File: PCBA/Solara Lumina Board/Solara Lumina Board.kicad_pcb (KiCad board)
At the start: 2 copper layers, 72.5 x 54 mm, 0 parts

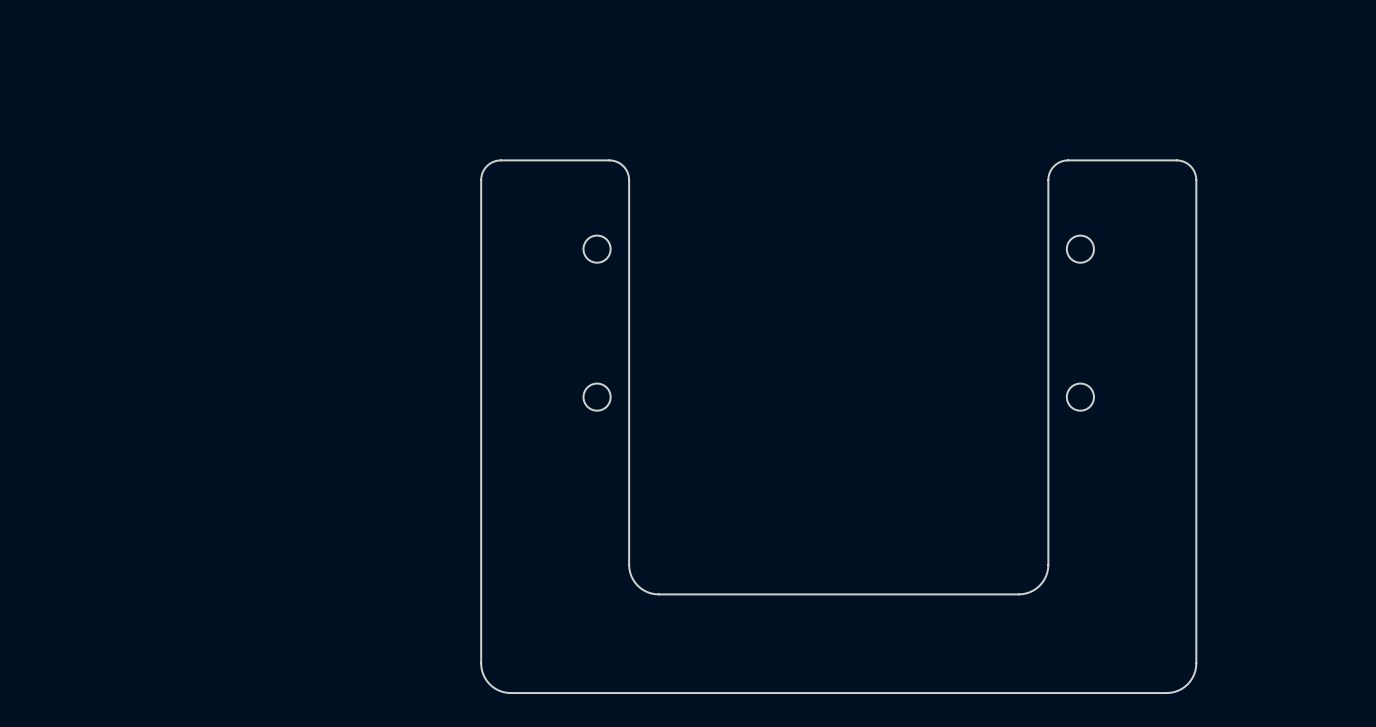
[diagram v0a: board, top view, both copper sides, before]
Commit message: Updated outline
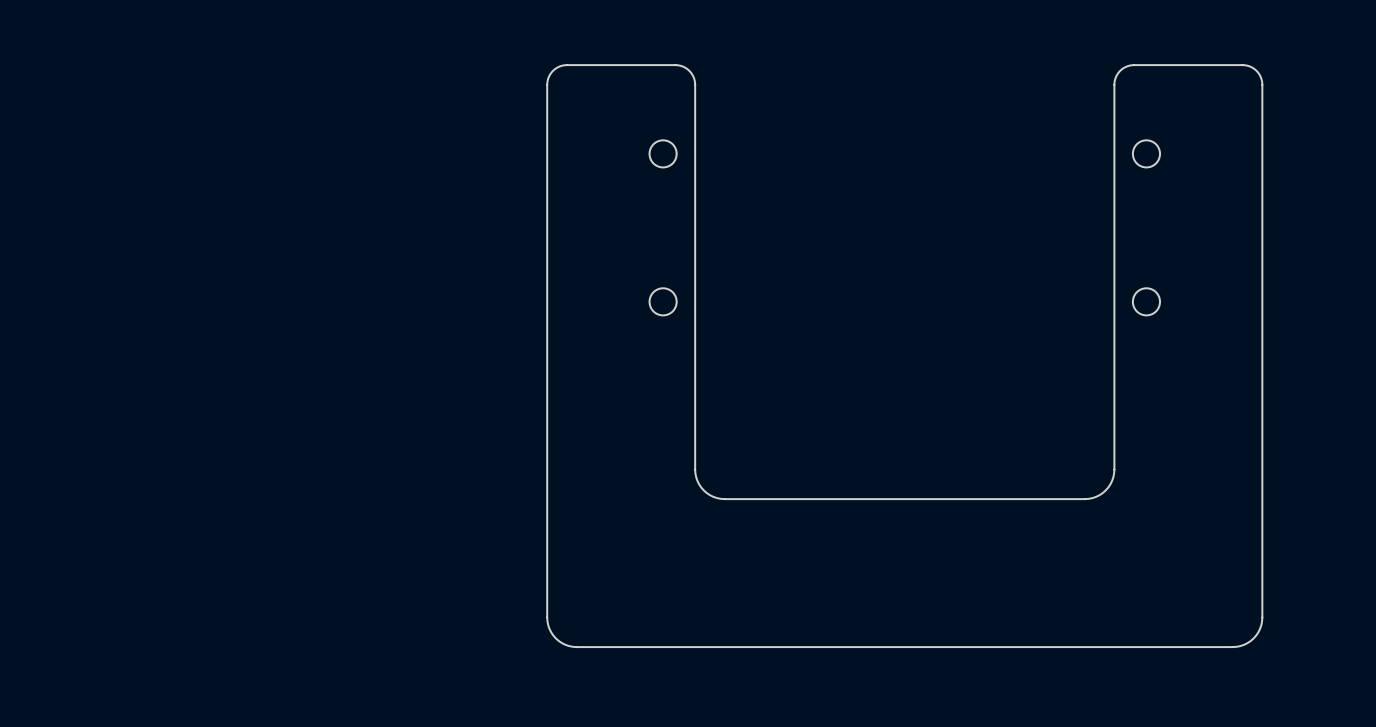
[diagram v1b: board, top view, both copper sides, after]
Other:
- board size 72.5 x 54 mm -> 72.5 x 59 mm
- copper layers 2 -> 6
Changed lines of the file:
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@@
 	(layers
 		(0 "F.Cu" signal)
+		(1 "In1.Cu" signal)
+		(2 "In2.Cu" signal)
+		(3 "In3.Cu" signal)
+		(4 "In4.Cu" signal)
 		(31 "B.Cu" signal)
 		(32 "B.Adhes" user "B.Adhesive")
@@
 	)
 	(setup
+		(stackup
+			(layer "F.SilkS"
+				(type "Top Silk Screen")
+			)
+			(layer "F.Paste"
+				(type "Top Solder Paste")
+			)
+			(layer "F.Mask"
+				(type "Top Solder Mask")
+				(color "White")
+				(thickness 0.01)
+			)
+			(layer "F.Cu"
+				(type "copper")
+				(thickness 0.035)
+			)
+			(layer "dielectric 1"
+				(type "prepreg")
+				(thickness 0.1)
+				(material "FR4")
+				(epsilon_r 4.5)
+				(loss_tangent 0.02)
+			)
+			(layer "In1.Cu"
+				(type "copper")
+				(thickness 0.035)
+			)
+			(layer "dielectric 2"
+				(type "core")
+				(thickness 0.535)
+				(material "FR4")
+				(epsilon_r 4.5)
+				(loss_tangent 0.02)
+			)
+			(layer "In2.Cu"
+				(type "copper")
+				(thickness 0.035)
+			)
+			(layer "dielectric 3"
+				(type "prepreg")
+				(thickness 0.1)
+				(material "FR4")
+				(epsilon_r 4.5)
+				(loss_tangent 0.02)
+			)
+			(layer "In3.Cu"
+				(type "copper")
+				(thickness 0.035)
+			)
+			(layer "dielectric 4"
+				(type "core")
+				(thickness 0.535)
+				(material "FR4")
+				(epsilon_r 4.5)
+				(loss_tangent 0.02)
+			)
+			(layer "In4.Cu"
+				(type "copper")
+				(thickness 0.035)
+			)
+			(layer "dielectric 5"
+				(type "prepreg")
+				(thickness 0.1)
+				(material "FR4")
+				(epsilon_r 4.5)
+				(loss_tangent 0.02)
+			)
+			(layer "B.Cu"
+				(type "copper")
+				(thickness 0.035)
+			)
+			(layer "B.Mask"
+				(type "Bottom Solder Mask")
+				(color "White")
+				(thickness 0.01)
+			)
+			(layer "B.Paste"
+				(type "Bottom Solder Paste")
+			)
+			(layer "B.SilkS"
+				(type "Bottom Silk Screen")
+			)
+			(copper_finish "None")
+			(dielectric_constraints no)
+		)
 		(pad_to_mask_clearance 0)
 		(allow_soldermask_bridges_in_footprints no)
@@
 	(net 0 "")
 	(gr_line
-		(start 177.18 71.660002)
-		(end 166.18 71.660002)
-		(stroke
-			(width 0.2)
-			(type default)
-		)
-		(layer "Edge.Cuts")
-	)
-	(gr_line
-		(start 164.18 73.660002)
-		(end 164.18 112.660002)
+		(start 167.875 106)
+		(end 131.375001 106)
+		(stroke
+			(width 0.2)
+			(type default)
+		)
+		(layer "Edge.Cuts")
+	)
+	(gr_arc
+		(start 116.375001 121)
+		(mid 114.25368 120.12132)
+		(end 113.375 117.999999)
+		(stroke
+			(width 0.2)
+			(type default)
+		)
+		(layer "Edge.Cuts")
+	)
+	(gr_arc
+		(start 126.375001 62)
+		(mid 127.789214 62.585786)
+		(end 128.375 63.999999)
+		(stroke
+			(width 0.2)
+			(type default)
+		)
+		(layer "Edge.Cuts")
+	)
+	(gr_arc
+		(start 131.375001 106)
+		(mid 129.25368 105.12132)
+		(end 128.375 102.999999)
+		(stroke
+			(width 0.2)
+			(type default)
+		)
+		(layer "Edge.Cuts")
+	)
+	(gr_arc
+		(start 183.875 62)
+		(mid 185.289214 62.585786)
+		(end 185.875 64)
+		(stroke
+			(width 0.2)
+			(type default)
+		)
+		(layer "Edge.Cuts")
+	)
+	(gr_line
+		(start 183.875 62)
+		(end 172.875 62)
+		(stroke
+			(width 0.2)
+			(type default)
+		)
+		(layer "Edge.Cuts")
+	)
+	(gr_line
+		(start 170.875 64)
+		(end 170.875 103)
+		(stroke
+			(width 0.2)
+			(type default)
+		)
+		(layer "Edge.Cuts")
+	)
+	(gr_arc
+		(start 170.875 103)
+		(mid 169.99632 105.12132)
+		(end 167.875 106)
 		(stroke
 			(width 0.2)
@@
 	)
 	(gr_circle
-		(center 118.43 80.660002)
-		(end 119.805 80.660002)
+		(center 174.125 71)
+		(end 175.5 71)
 		(stroke
 			(width 0.2)
@@
 		(layer "Edge.Cuts")
 	)
-	(gr_arc
-		(start 119.680001 71.660002)
-		(mid 121.094214 72.245788)
-		(end 121.68 73.660001)
-		(stroke
-			(width 0.2)
-			(type default)
-		)
-		(layer "Edge.Cuts")
-	)
-	(gr_arc
-		(start 106.68 73.66)
-		(mid 107.265786 72.245788)
-		(end 108.679998 71.660002)
-		(stroke
-			(width 0.2)
-			(type default)
-		)
-		(layer "Edge.Cuts")
-	)
-	(gr_line
-		(start 179.18 122.660002)
-		(end 179.18 73.660002)
-		(stroke
-			(width 0.2)
-			(type default)
-		)
-		(layer "Edge.Cuts")
-	)
-	(gr_line
-		(start 109.680001 125.660002)
-		(end 176.18 125.660002)
+	(gr_line
+		(start 185.875 118)
+		(end 185.875 64)
+		(stroke
+			(width 0.2)
+			(type default)
+		)
+		(layer "Edge.Cuts")
+	)
+	(gr_arc
+		(start 185.875 118)
+		(mid 184.99632 120.12132)
+		(end 182.875 121)
+		(stroke
+			(width 0.2)
+			(type default)
+		)
+		(layer "Edge.Cuts")
+	)
+	(gr_line
+		(start 113.375 63.999999)
+		(end 113.375 117.999999)
+		(stroke
+			(width 0.2)
+			(type default)
+		)
+		(layer "Edge.Cuts")
+	)
+	(gr_arc
+		(start 170.875 64)
+		(mid 171.460786 62.585786)
+		(end 172.875 62)
+		(stroke
+			(width 0.2)
+			(type default)
+		)
+		(layer "Edge.Cuts")
+	)
+	(gr_line
+		(start 116.375001 121)
+		(end 182.875 121)
+		(stroke
+			(width 0.2)
+			(type default)
+		)
+		(layer "Edge.Cuts")
+	)
+	(gr_line
+		(start 128.375 102.999999)
+		(end 128.375 63.999999)
+		(stroke
+			(width 0.2)
+			(type default)
+		)
+		(layer "Edge.Cuts")
+	)
+	(gr_arc
+		(start 113.375 63.999999)
+		(mid 113.960786 62.585786)
+		(end 115.374998 62)
 		(stroke
 			(width 0.2)
@@
 	)
 	(gr_circle
-		(center 167.43 95.660002)
-		(end 168.805 95.660002)
+		(center 125.125 86)
+		(end 126.5 86)
 		(stroke
 			(width 0.2)
@@
 		(layer "Edge.Cuts")
 	)
-	(gr_line
-		(start 121.68 112.660001)
-		(end 121.68 73.660001)
-		(stroke
-			(width 0.2)
-			(type default)
-		)
-		(layer "Edge.Cuts")
-	)
-	(gr_arc
-		(start 179.18 122.660002)
-		(mid 178.30132 124.781322)
-		(end 176.18 125.660002)
-		(stroke
-			(width 0.2)
-			(type default)
-		)
-		(layer "Edge.Cuts")
-	)
-	(gr_line
-		(start 161.18 115.660002)
-		(end 124.680001 115.660002)
-		(stroke
-			(width 0.2)
-			(type default)
-		)
-		(layer "Edge.Cuts")
-	)
-	(gr_arc
-		(start 164.18 73.660002)
-		(mid 164.765786 72.245788)
-		(end 166.18 71.660002)
-		(stroke
-			(width 0.2)
-			(type default)
-		)
-		(layer "Edge.Cuts")
-	)
-	(gr_arc
-		(start 124.680001 115.660002)
-		(mid 122.55868 114.781322)
-		(end 121.68 112.660001)
-		(stroke
-			(width 0.2)
-			(type default)
-		)
-		(layer "Edge.Cuts")
-	)
-	(gr_line
-		(start 119.680001 71.660002)
-		(end 108.679998 71.660002)
-		(stroke
-			(width 0.2)
-			(type default)
-		)
-		(layer "Edge.Cuts")
-	)
-	(gr_arc
-		(start 164.18 112.660002)
-		(mid 163.30132 114.781322)
-		(end 161.18 115.660002)
-		(stroke
-			(width 0.2)
-			(type default)
-		)
-		(layer "Edge.Cuts")
-	)
-	(gr_line
-		(start 106.68 73.66)
-		(end 106.68 122.660001)
-		(stroke
-			(width 0.2)
-			(type default)
-		)
-		(layer "Edge.Cuts")
-	)
-	(gr_arc
-		(start 177.18 71.660002)
-		(mid 178.594214 72.245788)
-		(end 179.18 73.660002)
-		(stroke
-			(width 0.2)
-			(type default)
-		)
-		(layer "Edge.Cuts")
-	)
 	(gr_circle
-		(center 167.43 80.660002)
-		(end 168.805 80.660002)
+		(center 125.125 71)
+		(end 126.5 71)
 		(stroke
 			(width 0.2)
@@
 		(layer "Edge.Cuts")
 	)
+	(gr_line
+		(start 126.375001 62)
+		(end 115.374998 62)
+		(stroke
+			(width 0.2)
+			(type default)
+		)
+		(layer "Edge.Cuts")
+	)
 	(gr_circle
-		(center 118.43 95.660002)
-		(end 119.805 95.660002)
+		(center 174.125 86)
+		(end 175.5 86)
 		(stroke
 			(width 0.2)
@@
 		(layer "Edge.Cuts")
 	)
-	(gr_arc
-		(start 109.680001 125.660002)
-		(mid 107.55868 124.781322)
-		(end 106.68 122.660001)
-		(stroke
-			(width 0.2)
-			(type default)
-		)
-		(layer "Edge.Cuts")
-	)

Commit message: Added ESP32-C6 and increased board size
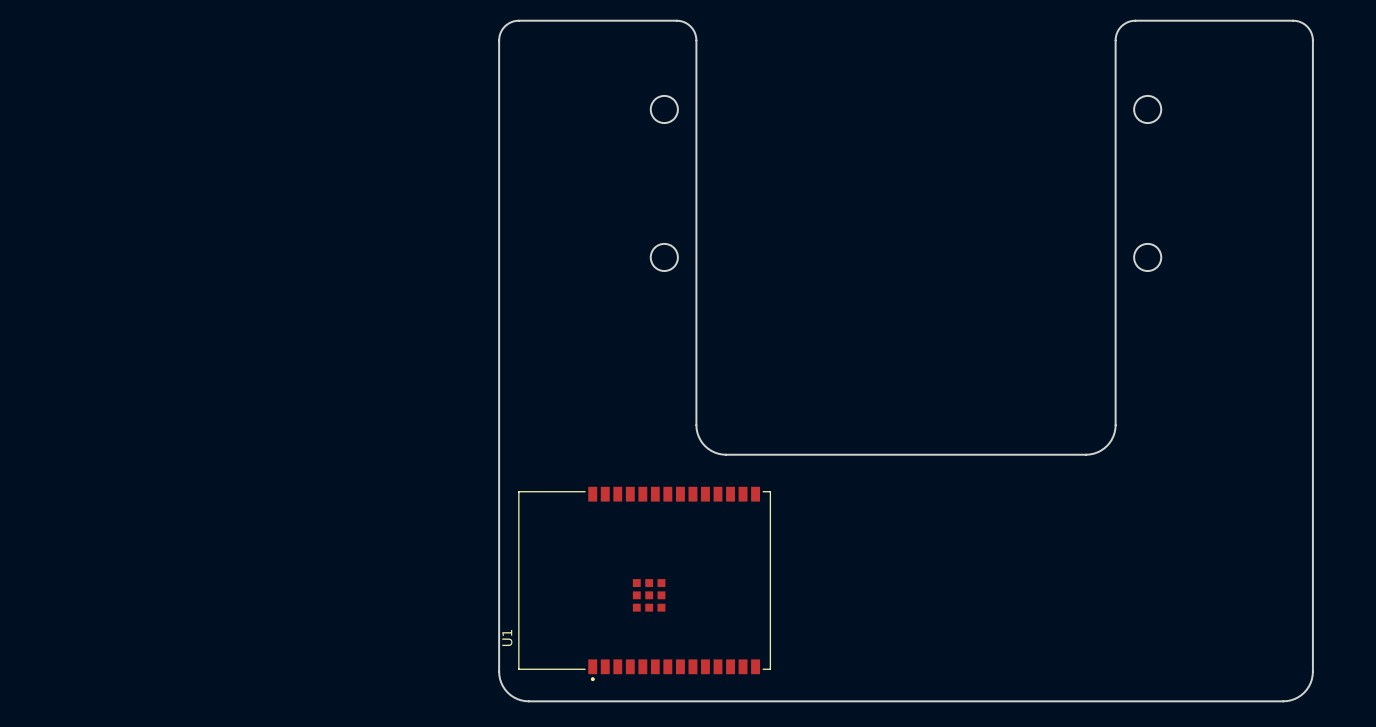
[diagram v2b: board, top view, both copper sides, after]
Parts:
- added U1: ESP32-C6-WROOM-1-N8, ClementsFootprints:ESP32-C6-WROOM-1-N8, F.Cu at (123.2, 114.2)
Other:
- board size 72.5 x 59 mm -> 82.5 x 69 mm

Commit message: Adding parts!
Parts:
- added D1: TEMD6200FX01, ClementsFootprints:PhotoDiode-0805, F.Cu at (149.7, 68.5)
- added TH1: P0K1.520.6W.A.010, Connector_PinHeader_2.00mm:PinHeader_1x02_P2.00mm_Vertical, F.Cu at (145.6, 69.0)
- added TH1: P0K1.520.6W.A.010, Connector_PinHeader_2.00mm:PinHeader_1x02_P2.00mm_Vertical, F.Cu at (161.5, 86.5)
- added U2: LM5169FDDAR, Package_SO:TI_SO-PowerPAD-8, F.Cu at (157.1, 81.3)
- added U3: ADS1015IDGS, Package_SO:TSSOP-10_3x3mm_P0.5mm, F.Cu at (156.0, 86.8)

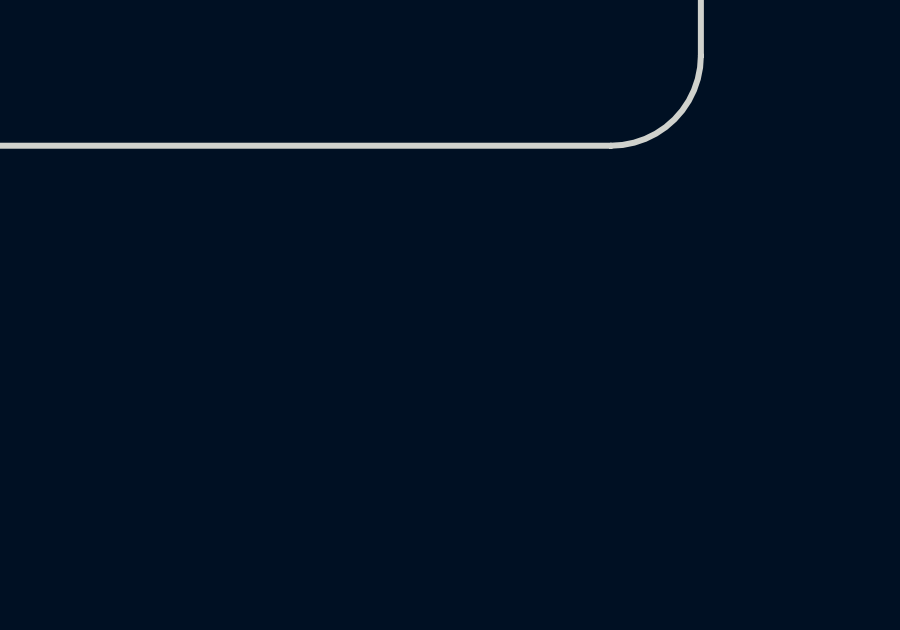
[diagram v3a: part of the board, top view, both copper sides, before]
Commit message: Added the op-amp eek
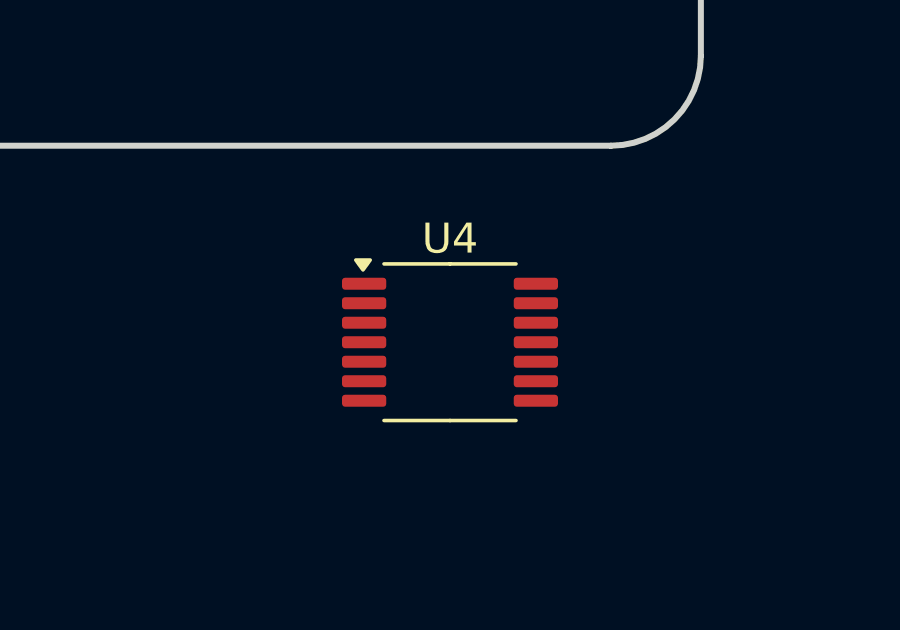
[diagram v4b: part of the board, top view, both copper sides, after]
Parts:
- added U4: MCP6009T-E/ST, Package_SO:TSSOP-14_4.4x5mm_P0.65mm, F.Cu at (162.6, 108.0)

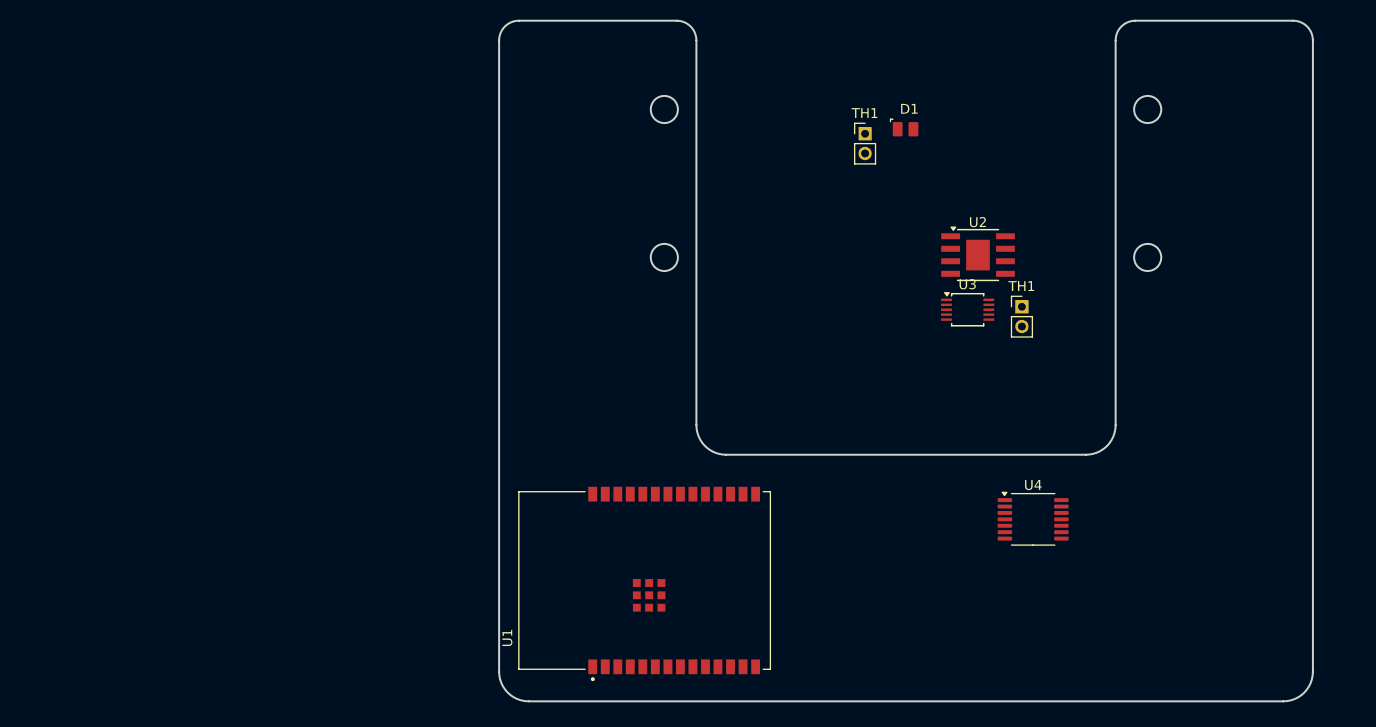
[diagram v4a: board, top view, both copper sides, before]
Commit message: Added more parts and adjusted board outline
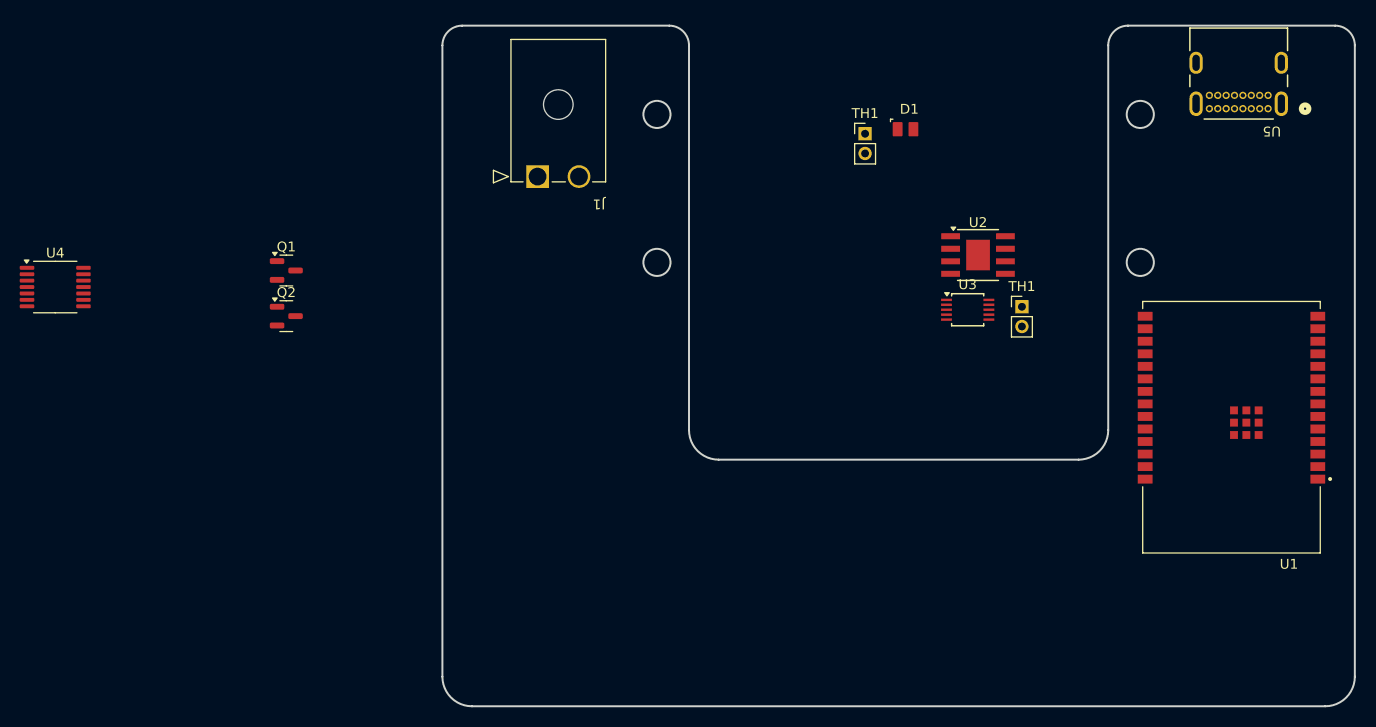
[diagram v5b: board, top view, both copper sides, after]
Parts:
- added J1: 1726480102, ClementsFootprints:Molex_1726480102, F.Cu at (114.5, 66.0)
- added Q1: 2N7002, Package_TO_SOT_SMD:SOT-23, F.Cu at (86.9, 82.8)
- added Q2: T2N7002AK,LM, Package_TO_SOT_SMD:SOT-23, F.Cu at (86.9, 87.5)
- added U5: 2137160001, ClementsFootprints:USB-C-2137160001, F.Cu at (186.5, 66.4)
- moved U4 101.9 mm to (63.5, 84.5)
- moved U1 61.5 mm to (182.7, 98.7), turned to 180 degrees
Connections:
- U4 pad 8: unconnected-(U4-Pad8) -> Net-(U4C--)
- U4 pad 9: unconnected-(U4C---Pad9) -> Net-(U4C--)
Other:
- board size 82.5 x 69 mm -> 92.5 x 69 mm
